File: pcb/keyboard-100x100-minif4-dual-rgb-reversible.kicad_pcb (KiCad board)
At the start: 2 copper layers, 100 x 100 mm, 101 parts, among them J1 TRRS, J2 TRRS, J3 Conn_01x04_Female, U1 MiniF4, U2 SN74LVC1T45DBV

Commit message: wip
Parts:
- added JP1: SolderJumper_3_Open, Jumper:SolderJumper-3_P1.3mm_Open_Pad1.0x1.5mm_NumberLabels, F.Cu at (110.1, 138.3)
- added JP2: SolderJumper_3_Open, Jumper:SolderJumper-3_P1.3mm_Open_Pad1.0x1.5mm_NumberLabels, F.Cu at (140.2, 137.7)
- added JP3: SolderJumper_2_Open, Jumper:SolderJumper-2_P1.3mm_Open_Pad1.0x1.5mm, F.Cu at (113.5, 139.0)
- added SW_BOOT0: SW_Push, ProjectLocal:switch_3x6, F.Cu at (162.6, 141.3)
- added SW_RESET1: SW_Push, ProjectLocal:switch_3x6, F.Cu at (167.6, 141.2)
- U1: value MiniF4 -> Conn_02x20_Top_Bottom; footprint ProjectLocal:WeAct_MiniF4_ZigZag -> ProjectLocal:DIP40_Reversible_ZigZag
- moved H14 18.7 mm to (103.8, 122.8)
- moved H2 18.7 mm to (103.8, 122.8)
- moved R5 5.99 mm to (164.7, 134.4), turned to 180 degrees
- moved R3 4.97 mm to (105.2, 116.0), turned to 180 degrees
- moved R6 1.66 mm to (164.7, 137.4), turned to 180 degrees
- renumbered JP7 to JP10, JP8 to JP11, JP9 to JP12, JP10 to JP13, JP1 to JP4, JP2 to JP5, JP3 to JP6, JP4 to JP7, JP5 to JP8, JP6 to JP9
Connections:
- U1 pad 1: Net-(U1-Pad1) -> /RE_A
- U1 pad 10: /RGB_DIN_3V3 -> /SW22
- U1 pad 11: /SW31 -> /SW23
- U1 pad 12: /SW15 -> /SW24
- U1 pad 13: /SW43 -> /SW21
- U1 pad 14: /SW42 -> /SCL_TX
- U1 pad 15: /SW41 -> /SDA_RX
- U1 pad 16: /SW35 -> /OLED_SCL
- U1 pad 17: /SW34 -> /OLED_SDA
- U1 pad 18: /SW33 -> /5V
- U1 pad 19: /SW32 -> /GND
- U1 pad 2: Net-(U1-Pad2) -> /RE_B
- U1 pad 20: Net-(U1-Pad20) -> /3V3
- U1 pad 21: /SW25 -> (no net)
- U1 pad 25: /RE_A -> /NC_or_BOOT0
- U1 pad 26: /RE_B -> /SW32
- U1 pad 27: /SW_RE -> /SW33
- U1 pad 28: /SW11 -> /SW34
- U1 pad 29: /SW12 -> /SW35
- U1 pad 3: Net-(U1-Pad3) -> /SW_RE
- U1 pad 30: /SW13 -> /SW41
- U1 pad 31: /SW14 -> /SW42
- U1 pad 32: Net-(U1-Pad32) -> /SW43
- U1 pad 33: Net-(U1-Pad33) -> /SW15
- U1 pad 38: /SW22 -> (no net)
- U1 pad 39: /SW23 -> (no net)
- U1 pad 4: Net-(U1-Pad4) -> /SW11
- U1 pad 40: /SW24 -> (no net)
- U1 pad 7: Net-(U1-Pad7) -> /SW14
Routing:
- net /5V: track 1091.6 -> 1005.3 mm
- net /RESET: track 0.00 -> 67.6 mm, vias 0 -> 5
- net /SW25: track 171.5 -> 123.0 mm, vias 7 -> 6
- net /GND: track 261.1 -> 227.1 mm, vias 60 -> 49
- net /OLED_SDA: track 48.6 -> 23.5 mm, vias 4 -> 1
- net /SW43: track 88.4 -> 68.5 mm, vias 3 -> 1
- net /SW15: track 171.1 -> 151.5 mm
- net /RESET_or_SW25: track 0.00 -> 19.4 mm, vias 0 -> 1
- net /SW35: track 122.8 -> 103.6 mm, vias 7 -> 5
- net /SW25_or_RESET: track 0.00 -> 18.3 mm, vias 0 -> 1
- net /NC_or_BOOT0: track 0.00 -> 18.1 mm, vias 0 -> 1
- net (no net): track 0.00 -> 17.9 mm
- net Net-(U1-Pad7): track 17.6 -> 0.00 mm, vias 1 -> 0
- net Net-(U1-Pad20): track 17.5 -> 0.00 mm, vias 1 -> 0
- net Net-(U1-Pad2): track 17.4 -> 0.00 mm, vias 1 -> 0
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
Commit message: wip
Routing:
- net /BOOT0: track 4.67 -> 60.4 mm, vias 1 -> 5
- net /SW25: track 123.0 -> 163.3 mm, vias 6 -> 9
- net /OLED_SDA: track 23.5 -> 52.0 mm, vias 1 -> 5
- net /SW15: track 151.5 -> 171.6 mm, vias 9 -> 13
- net /SDA_RX: track 102.0 -> 121.9 mm, vias 3 -> 5
- net /SW35: track 103.6 -> 123.5 mm, vias 5 -> 7
- net /SW43: track 68.5 -> 87.7 mm, vias 1 -> 5
- net (no net): track 17.9 -> 0.00 mm
- net /SCL_TX: track 107.4 -> 123.6 mm, vias 7 -> 9
- net /OLED_SCL: track 30.5 -> 45.1 mm, vias 2 -> 4
- net /GND: track 227.1 -> 239.3 mm, vias 49 -> 50
- net Net-(D_BL_1-Pad4): track 63.5 -> 69.2 mm
- net /RESET: track 67.6 -> 70.2 mm, vias 5 -> 6
- net /SW14: track 160.3 -> 162.7 mm

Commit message: wip
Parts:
- removed H1, H2, H3, H4, H5: MountingHole, ProjectLocal:Bumpon_3M_F0502
- added C1: 100nF, ProjectLocal:C_0805_2012Metric_Pad1.18x1.45mm_HandSolder_Dual, F.Cu at (141.1, 124.6)
- added C2: 100nF, ProjectLocal:C_0805_2012Metric_Pad1.18x1.45mm_HandSolder_Dual, F.Cu at (141.1, 126.6)
- BOOT0: renamed from SW_BOOT0; footprint ProjectLocal:switch_3x6 -> ProjectLocal:SW_Push_SPST_3x6mm
- RESET: renamed from SW_RESET1; footprint ProjectLocal:switch_3x6 -> ProjectLocal:SW_Push_SPST_3x6mm
- moved H11 13.3 mm to (191.6, 52.6)
- moved JP2 0.65 mm to (140.2, 138.3)
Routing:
- net /RE_A: track 48.7 -> 57.2 mm
- net /SCL_TX: track 123.6 -> 117.3 mm, vias 9 -> 8
- net /RE_B: track 49.3 -> 52.3 mm
- net /SDA_RX: track 121.9 -> 119.2 mm
- net /BOOT0: track 60.4 -> 59.1 mm, vias 5 -> 3
- net /5V: track 1005.3 -> 1004.1 mm
- net /SW21: track 76.2 -> 75.1 mm
- net /SW35: track 123.5 -> 124.5 mm
- net /SW25: track 163.3 -> 164.3 mm
- net /SW43: track 87.7 -> 88.6 mm
- net /SW15: track 171.6 -> 172.5 mm, vias 13 -> 9
- net /SW41: track 53.2 -> 53.9 mm
- net /SW25_or_RESET: track 18.3 -> 18.9 mm
- net /GND: track 239.3 -> 239.6 mm, vias 50 -> 49
- net /3V3: vias 6 -> 4
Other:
- board text added: "11"
- board text added: "12"
- board text added: "13"
- board text added: "14"
- board text added: "15"
- board text added: "21"
- board text added: "22"
- board text added: "23"
- board text added: "24"
- board text added: "25"
- board text added: "31"
- board text added: "32"
- board text added: "33"
- board text added: "34"
- board text added: "35"
- board text added: "41"
- board text added: "42"
- board text added: "43"
- board text added: "B6"
- board text added: "B7"
- board text added: "Bluepill"
- board text added: "CL"
- board text added: "DA"
- board text added: "G"
- board text added: "L"
- board text added: "MiniF4"
- board text added: "R"
- board text added: "RE"
- board text added: "github.com/rgoulter rev. 2021.5"
- board text removed: "OLED SCL"
- board text removed: "OLED SDA"
- board text removed: "RE_A"
- board text removed: "RE_B"
- board text removed: "RGB"
- board text removed: "SCL/TX"
- board text removed: "SDA/RX"
- board text removed: "SW11"
- board text removed: "SW12"
- board text removed: "SW13"
- board text removed: "SW14"
- board text removed: "SW15"
- board text removed: "SW21"
- board text removed: "SW22"
- board text removed: "SW23"
- board text removed: "SW24"
- board text removed: "SW25"
- board text removed: "SW31"
- board text removed: "SW32"
- board text removed: "SW33"
- board text removed: "SW34"
- board text removed: "SW35"
- board text removed: "SW41"
- board text removed: "SW42"
- board text removed: "SW43"
- board text removed: "SW_RE"
- board text removed: "github.com/rgoulter rev. 2021.4"

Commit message: wip; need some rerouting
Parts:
- removed H14, H15: MountingHole, MountingHole:MountingHole_2.2mm_M2_ISO7380_Pad
- added H1: MountingHole, ProjectLocal:Bumpon_3M_F0502, F.Cu at (31.5, 120.5)
- added H2: MountingHole, ProjectLocal:Bumpon_3M_F0502, F.Cu at (39.4, 119.9)
- added H3: MountingHole, ProjectLocal:Bumpon_3M_F0502, F.Cu at (46.6, 120.0)
- added H4: MountingHole, ProjectLocal:Bumpon_3M_F0502, F.Cu at (53.7, 120.4)
- added H5: MountingHole, ProjectLocal:Bumpon_3M_F0502, F.Cu at (60.2, 121.5)
- added M1: Motor_DC, ProjectLocal:Mini_DC_Motor, F.Cu at (167.0, 112.5)
- added Q1: Q_NPN_BCE, ProjectLocal:SOT-23_Handsoldering_Reversible, F.Cu at (181.0, 112.8)
- added R7: 500R, ProjectLocal:Resistor-Hybrid, F.Cu at (179.7, 108.1)
- added R8: 500R, ProjectLocal:Resistor-Hybrid, F.Cu at (179.8, 117.1)
- JP1, JP2: value SolderJumper_3_Open -> SolderJumper_3_Bridged12; footprint Jumper:SolderJumper-3_P1.3mm_Open_Pad1.0x1.5mm_NumberLabels -> Jumper:SolderJumper-3_P1.3mm_Bridged2Bar12_RoundedPad1.0x1.5mm_NumberLabels
- JP3: value SolderJumper_2_Open -> SolderJumper_2_Bridged; footprint Jumper:SolderJumper-2_P1.3mm_Open_Pad1.0x1.5mm -> Jumper:SolderJumper-2_P1.3mm_Bridged2Bar_RoundedPad1.0x1.5mm
- U1: value Conn_02x20_Top_Bottom -> BluePill_or_MiniF4
- moved H11 111.9 mm to (105.0, 123.5)
- moved H12 88.1 mm to (159.5, 129.5)
- moved H13 61.2 mm to (159.5, 147.5)
- turned JP1 to 90 degrees
- turned JP2 to 90 degrees
- renumbered BOOT0 to SW_BOOT0, RESET to SW_RESET1
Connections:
- JP1 pad 1: /RESET -> /SW25
- JP1 pad 3: /SW25 -> /RESET
- JP2 pad 1: /SW25 -> /RESET
- JP2 pad 3: /RESET -> /SW25
- U1 pad 21: (no net) -> /GND_or_5V
- U1 pad 34: /SW31 -> /MOTOR_PWM
- U1 pad 37: (no net) -> Net-(U1-Pad37)
- U1 pad 38: (no net) -> Net-(U1-Pad38)
- U1 pad 39: (no net) -> /SW31
- U1 pad 40: (no net) -> Net-(U1-Pad40)
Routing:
- net /SW31: track 57.9 -> 26.2 mm, vias 8 -> 5
- net /GND: track 239.6 -> 238.6 mm

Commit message: wip
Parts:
- moved C_BL_1 38.1 mm to (150.3, 173.6)
- moved D_BL_1 38.1 mm to (150.3, 168.4)
- moved SW_RESET1 22.4 mm to (172.2, 163.2)
- moved SW_BOOT0 22.4 mm to (167.2, 163.3)
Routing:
- net /SW35: track 124.5 -> 78.3 mm, vias 7 -> 5
- net /GND: track 238.6 -> 197.2 mm, vias 49 -> 44
- net /SW15: track 172.5 -> 131.9 mm
- net /SW25: track 164.3 -> 131.3 mm
- net /SW43: track 88.6 -> 56.5 mm, vias 5 -> 1
- net /SDA_RX: track 119.2 -> 91.0 mm, vias 5 -> 3
- net /SCL_TX: track 117.3 -> 89.3 mm, vias 8 -> 6
- net /5V: track 1004.1 -> 989.1 mm, vias 36 -> 35
- net /SW14: track 162.7 -> 147.8 mm
- net /SW24: track 110.5 -> 96.6 mm
- net /SW34: track 111.7 -> 100.3 mm
- net /RESET: track 70.5 -> 61.4 mm, vias 6 -> 5
- net Net-(D_BL_1-Pad4): track 69.2 -> 64.3 mm, vias 9 -> 8
- net /SW42: track 73.8 -> 77.8 mm
- net /DOUT_4: track 20.3 -> 17.0 mm, vias 3 -> 2
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
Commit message: iterate
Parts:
- moved Q1 7.93 mm to (176.8, 106.0)
- moved R7 5.08 mm to (179.8, 113.2), turned to 270 degrees
- moved R8 4.55 mm to (182.1, 113.2), turned to 270 degrees
- moved M1 1.31 mm to (165.9, 111.9)
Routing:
- net /5V: track 989.1 -> 1018.8 mm, vias 35 -> 39
- net /SW25: track 131.3 -> 101.6 mm, vias 9 -> 5
- net /SW34: track 100.3 -> 91.6 mm, vias 11 -> 9

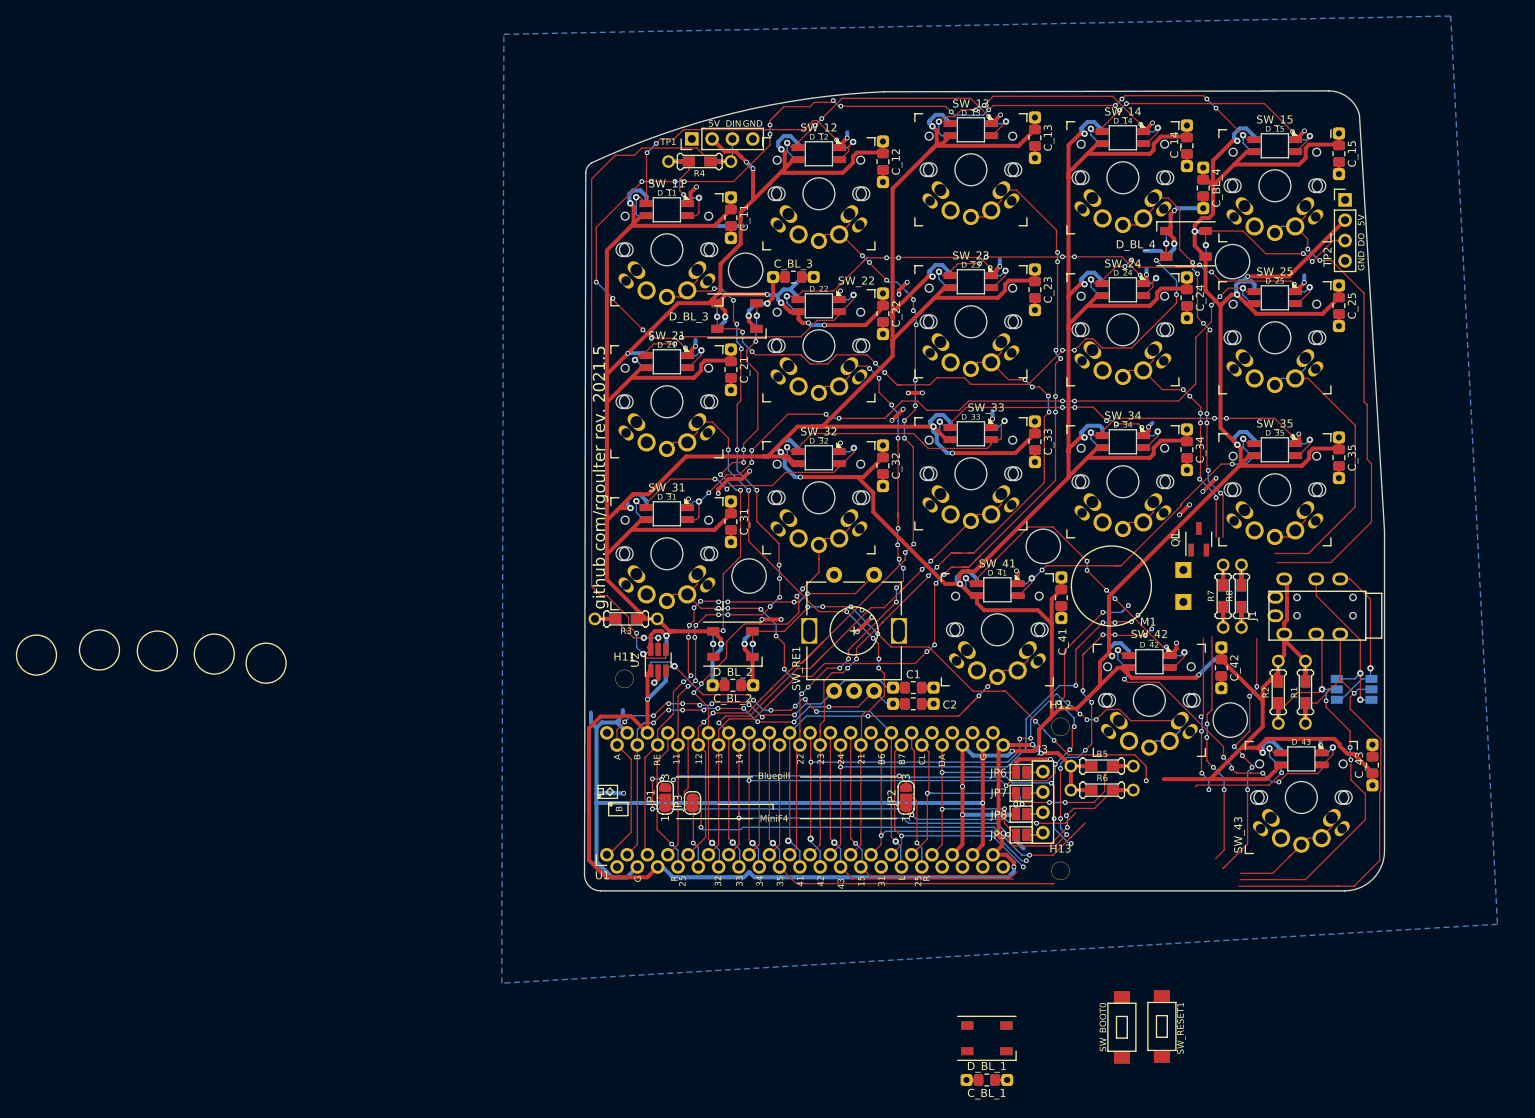
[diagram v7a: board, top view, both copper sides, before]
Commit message: mostly connected, but also very untidy
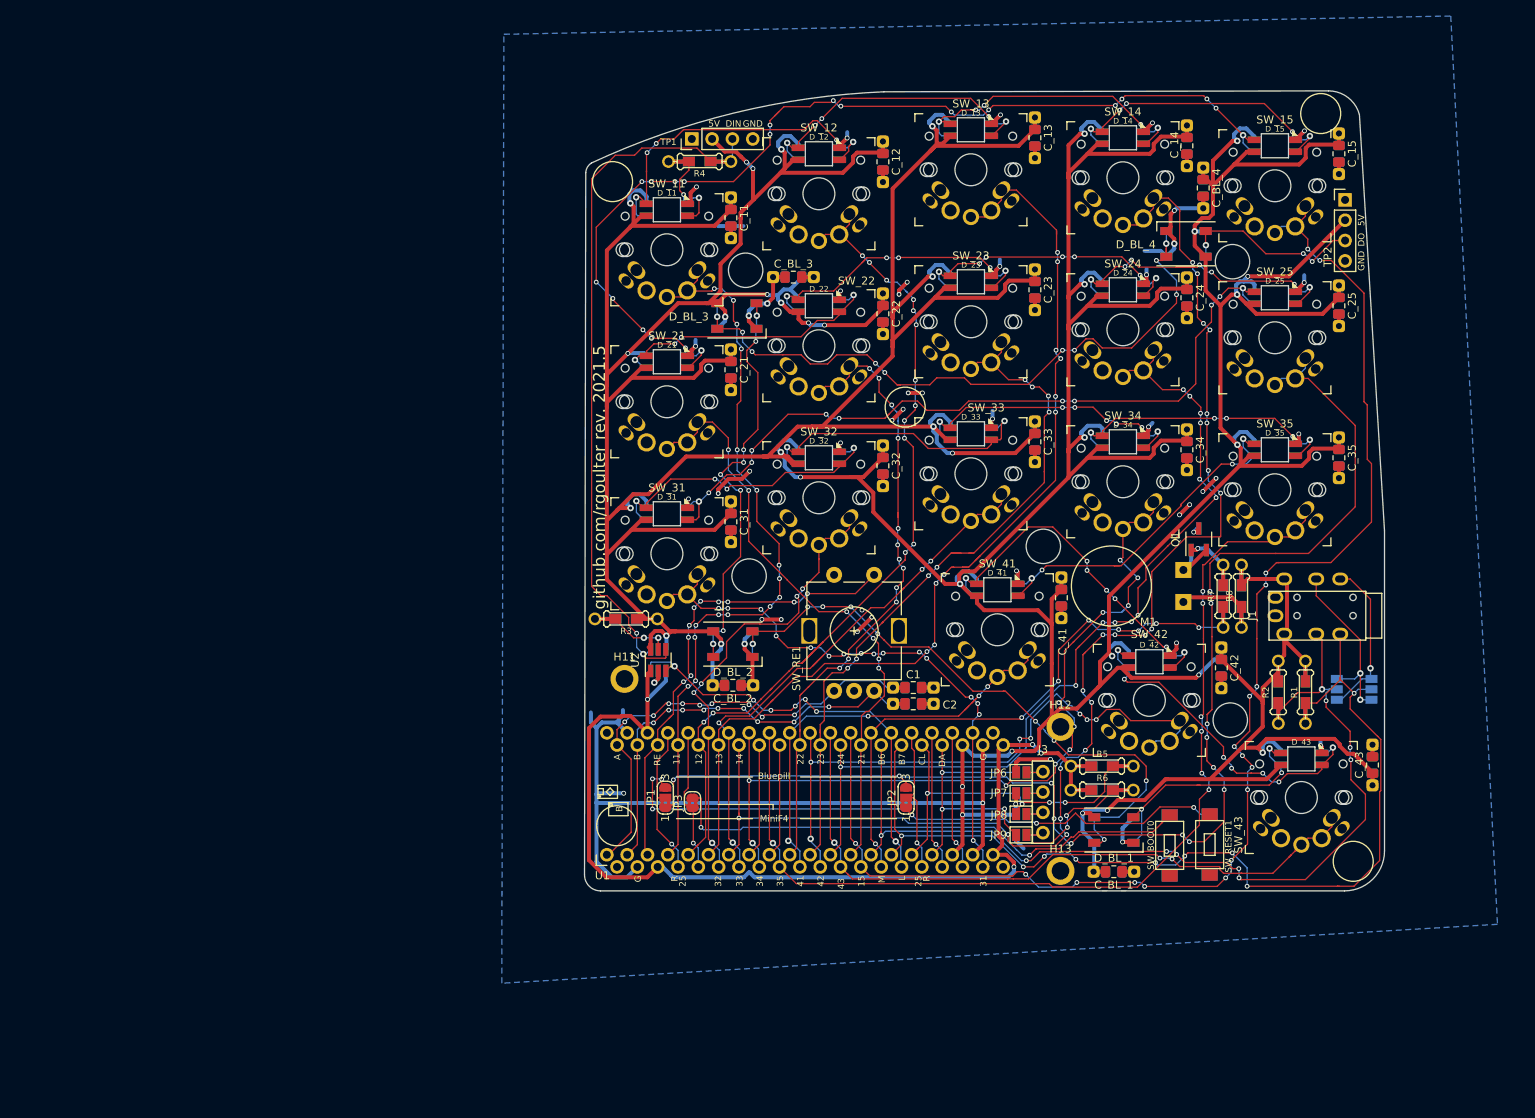
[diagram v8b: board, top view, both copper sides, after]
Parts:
- moved H1 166.6 mm to (196.1, 146.3)
- moved H3 160.2 mm to (192.0, 52.8)
- moved H2 105.2 mm to (140.1, 89.5)
- moved H4 77.2 mm to (103.5, 61.3)
- moved H5 48.3 mm to (104.0, 141.9)
- moved C_BL_1 30.5 mm to (166.2, 147.6)
- moved D_BL_1 30.5 mm to (166.2, 142.4)
- moved SW_RESET1 23.5 mm to (178.1, 140.4)
- moved SW_BOOT0 23.5 mm to (173.1, 140.5)
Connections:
- U1 pad 21: /GND_or_5V -> (no net)
- U1 pad 40: Net-(U1-Pad40) -> (no net)
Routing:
- net /MOTOR_PWM: track 0.00 -> 70.5 mm, vias 0 -> 8
- net /SW25: track 101.6 -> 165.3 mm, vias 5 -> 13
- net /SW35: track 78.3 -> 124.2 mm, vias 5 -> 7
- net /SW31: track 26.2 -> 70.9 mm, vias 5 -> 16
- net /SW15: track 131.9 -> 171.4 mm, vias 9 -> 17
- net /SDA_RX: track 91.0 -> 122.9 mm, vias 3 -> 9
- net /SW43: track 56.5 -> 87.4 mm, vias 1 -> 3
- net /SCL_TX: track 89.3 -> 118.8 mm, vias 6 -> 10
- net /RESET: track 61.4 -> 80.0 mm, vias 5 -> 6
- net /SW14: track 147.8 -> 165.2 mm
- net Net-(U1-Pad38): track 0.00 -> 17.3 mm, vias 0 -> 1
- net Net-(U1-Pad37): track 0.00 -> 17.3 mm, vias 0 -> 1
- net /DOUT_4: track 17.0 -> 31.3 mm, vias 2 -> 3
- net /SW24: track 96.6 -> 110.4 mm
- net Net-(D_BL_1-Pad4): track 64.3 -> 78.1 mm, vias 8 -> 9
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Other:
- board text added: "M"
